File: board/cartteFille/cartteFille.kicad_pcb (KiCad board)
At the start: 2 copper layers, 60 x 100 mm, 69 parts, among them U1 LM358, U20 MCP23018, U21-2 SN74, U23-4 SN74, U25-6 SN74, U27-8 SN74

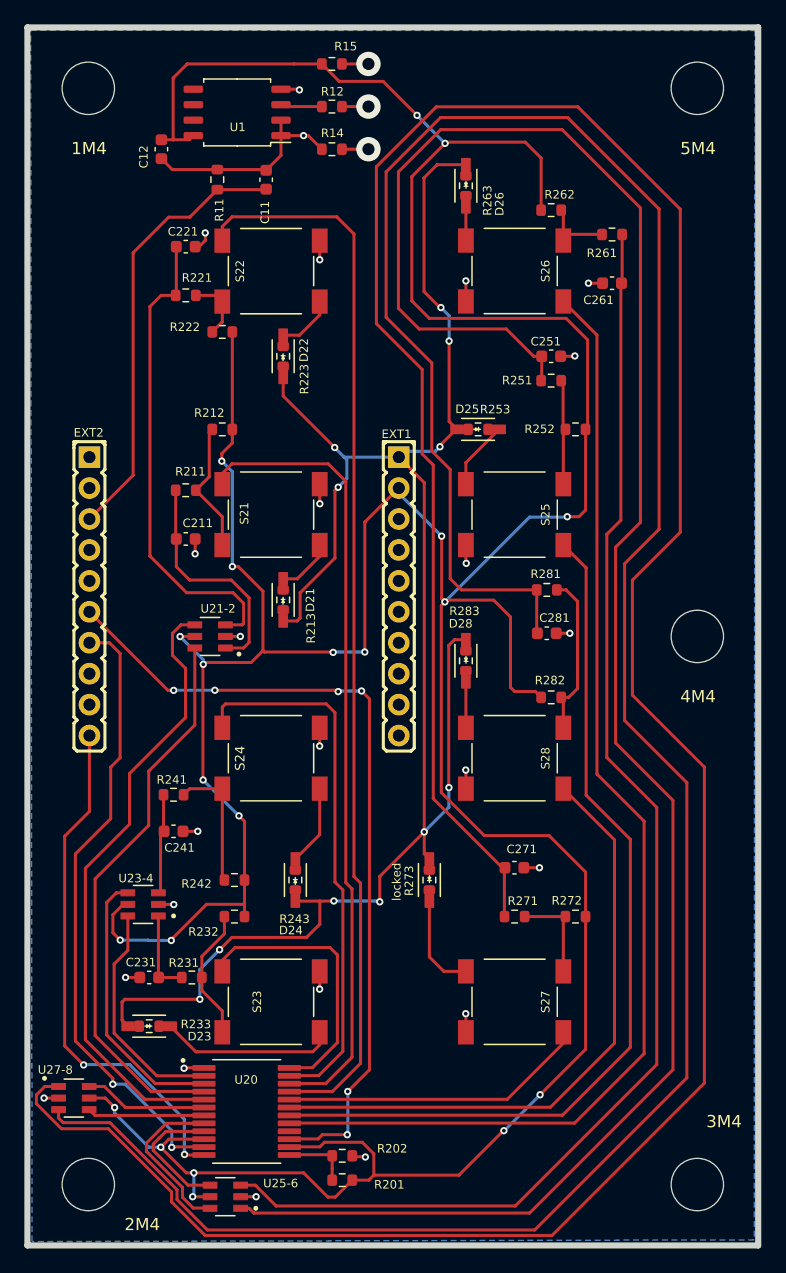
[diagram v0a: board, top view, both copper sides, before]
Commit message: Cangement Silkscreen pour JLCPCB
JLCPCB veut un minimum de 1mmx1mm pour le texte dans les silkscreen j£ai donc augmenter et replacer les Labels de la couche silkscreen
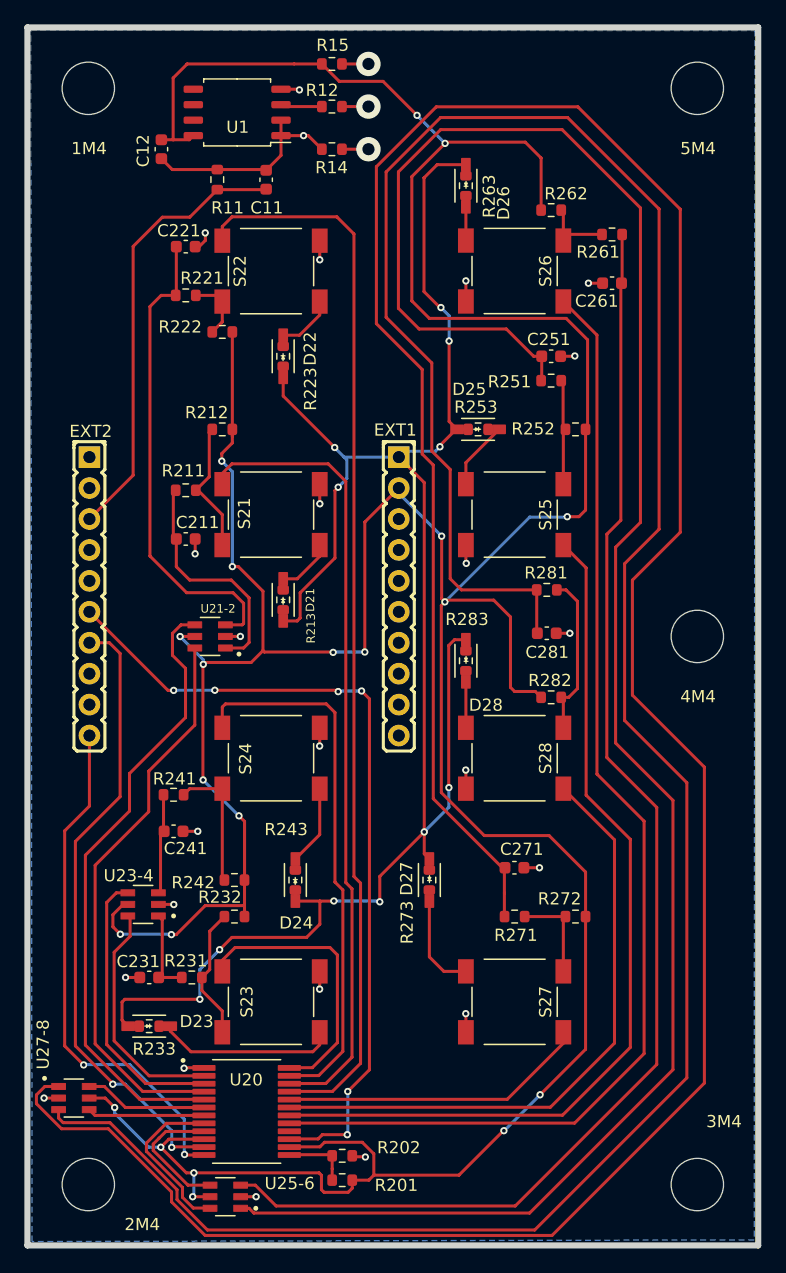
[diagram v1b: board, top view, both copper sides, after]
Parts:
- R272: value 1K -> 1KOhm
- renumbered locked to D27
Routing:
- net /U20GPB0-U234S23: track 18.9 -> 19.4 mm

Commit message: Clean_V1.0
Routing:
- net /GPIO32-INTB: track 67.4 -> 68.9 mm
- net Net-(C271-Pad1): track 240.2 -> 241.2 mm
- net /I2C_SDA: track 43.2 -> 43.9 mm
- net /U20GPB3-U212S22: track 51.4 -> 50.8 mm

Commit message: Send_to_review_V1.0
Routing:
- net /ADC_CH0-U11RP1: track 36.7 -> 37.5 mm
- net GND: track 49.0 -> 48.5 mm
